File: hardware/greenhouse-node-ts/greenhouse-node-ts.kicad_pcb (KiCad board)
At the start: 4 copper layers, 70 x 50 mm, 31 parts, among them J1 Conn_01x12_Male, J3 Conn_01x02_Pin, J7 Conn_01x04_Pin, SW1 SW_Push, U5 STM32F030F4P6, U7 PCF8574ATS/3,118, U8 XC6706x, U9 RFM69HW

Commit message: Fixed cap sizes, generated BOMs
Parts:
- C14, C16: footprint Capacitor_THT:C_Disc_D4.7mm_W2.5mm_P5.00mm -> Capacitor_THT:C_Disc_D3.0mm_W2.0mm_P2.50mm
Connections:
- C1 pad 1: unconnected-(C1-Pad1) -> GND

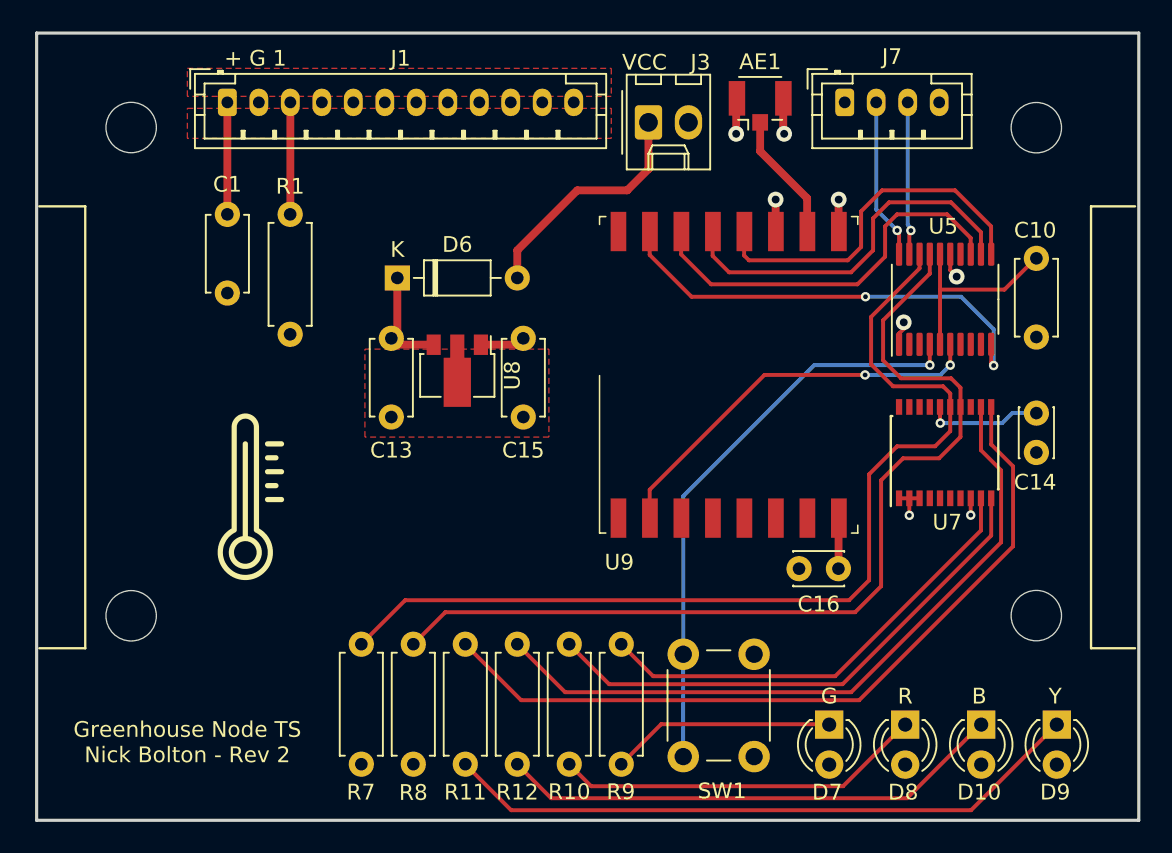
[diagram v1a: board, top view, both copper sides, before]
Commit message: Improved schematics
Add todos, test points, fixed PCF8574 symbol,
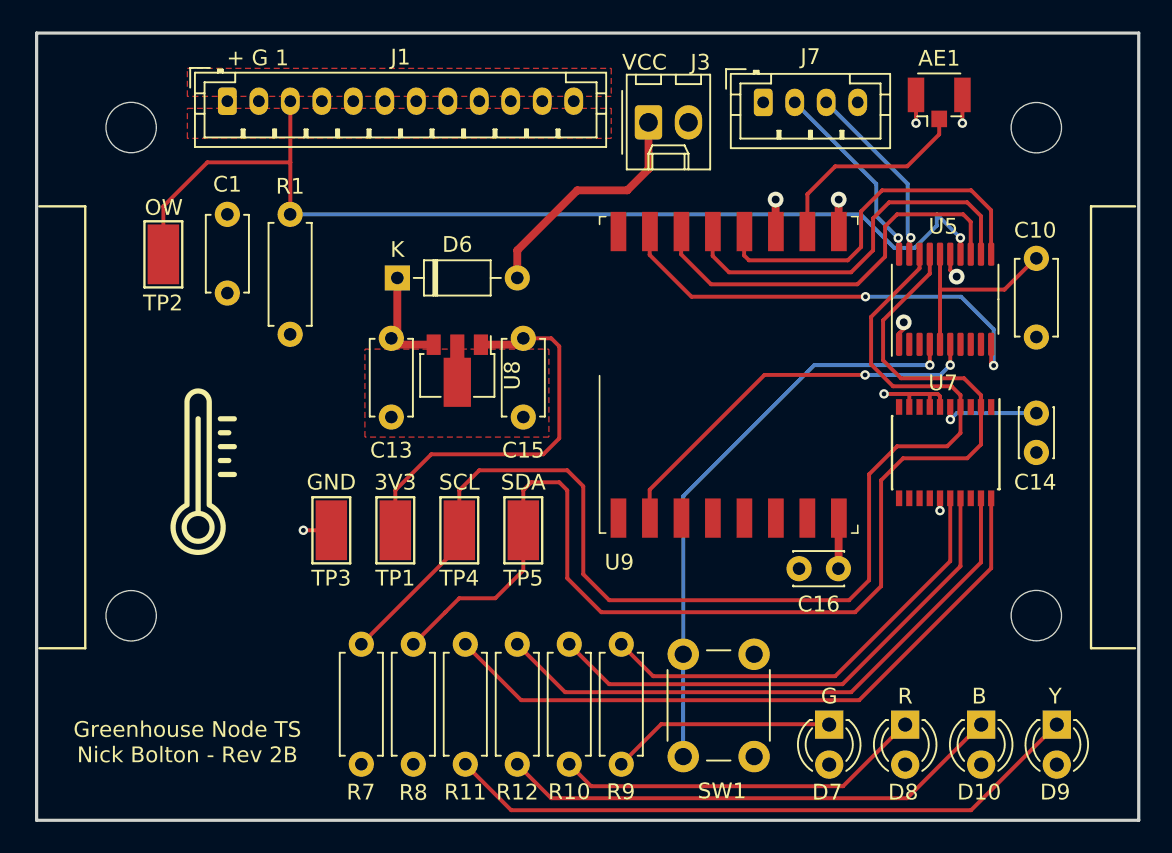
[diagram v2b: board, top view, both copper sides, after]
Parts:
- added TP1: 3V3, TestPoint:TestPoint_Keystone_5019_Minature, F.Cu at (90.7, 67.3)
- added TP2: OW, TestPoint:TestPoint_Keystone_5019_Minature, F.Cu at (75.9, 49.8)
- added TP3: GND, TestPoint:TestPoint_Keystone_5019_Minature, F.Cu at (86.6, 67.3)
- added TP4: SCL, TestPoint:TestPoint_Keystone_5019_Minature, F.Cu at (94.7, 67.3)
- added TP5: SDA, TestPoint:TestPoint_Keystone_5019_Minature, F.Cu at (98.8, 67.3)
- J1: value Conn_01x12_Male -> Conn_01x12_Pin
- moved AE1 11.4 mm to (125.2, 40.1)
- moved J7 5.18 mm to (114.0, 40.1)
- moved J1 0.08 mm to (80.0, 40.1)
- turned U7 to -90 degrees
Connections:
- J1 pad 12: /OneWire -> /OW
- J1 pad 3: /OneWire -> /OW
- J1 pad 6: /OneWire -> /OW
- J1 pad 9: /OneWire -> /OW
- R1 pad 2: /OneWire -> /OW
- U5 pad 14: unconnected-(U5-PB1-Pad14) -> /OW
- U7 pad 1: GND -> unconnected-(U7-~{INT}-Pad1)
- U7 pad 10: /LED_R -> unconnected-(U7-P0-Pad10)
- U7 pad 11: /LED_Y -> unconnected-(U7-P1-Pad11)
- U7 pad 12: /LED_B -> unconnected-(U7-P2-Pad12)
- U7 pad 14: /SCL -> unconnected-(U7-P3-Pad14)
- U7 pad 15: /SDA -> GND
- U7 pad 16: +3V3 -> /LED_G
- U7 pad 17: (no net) -> /LED_R
- U7 pad 18: (no net) -> unconnected-(U7-NC-Pad18)
- U7 pad 19: (no net) -> /LED_B
- U7 pad 2: GND -> /SCL
- U7 pad 20: (no net) -> /LED_Y
- U7 pad 3: GND -> unconnected-(U7-NC-Pad3)
- U7 pad 4: unconnected-(U7-P0-Pad4) -> /SDA
- U7 pad 5: unconnected-(U7-P1-Pad5) -> +3V3
- U7 pad 6: unconnected-(U7-P2-Pad6) -> GND
- U7 pad 7: unconnected-(U7-P3-Pad7) -> GND
- U7 pad 8: GND -> unconnected-(U7-NC-Pad8)
- U7 pad 9: /LED_G -> GND
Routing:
- net /OW: track 0.00 -> 65.9 mm, vias 0 -> 1
- net /SCL: track 60.9 -> 76.6 mm
- net +3V3: track 33.3 -> 47.8 mm
- net /SDA: track 63.4 -> 76.9 mm
- net /OneWire: track 7.05 -> 0.00 mm
- net /LED_Y: track 49.7 -> 42.8 mm
- net /LED_B: track 45.1 -> 38.2 mm
- net Net-(AE1-A): track 8.18 -> 13.3 mm
- net GND: track 15.0 -> 19.2 mm, vias 8 -> 9
- net /SWCLK: track 10.2 -> 12.4 mm
- net /SWDIO: track 9.77 -> 11.9 mm
- net /LED_R: track 34.1 -> 33.3 mm
- net /LED_G: track 29.6 -> 28.8 mm
- net /SCK: track 23.2 -> 23.8 mm
- net /MOSI: track 25.2 -> 25.8 mm
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- removed copper zone on F.Cu, net /OneWire
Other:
- board text added: "Greenhouse Node TS Nick Bolton - Rev 2B"
- board text removed: "Greenhouse Node TS Nick Bolton - Rev 2"
